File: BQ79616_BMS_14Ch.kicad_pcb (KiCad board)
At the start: 2 copper layers, 100 x 60 mm, 155 parts, among them J1 Conn_02x10_Odd_Even, J2 Conn_02x10_Odd_Even, J3 Conn_Therm, J4 BMS_A_IN, J5 BMS_A_OUT, Q1 MMBT5551

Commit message: Finish positioning of all components Ver1ST
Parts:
- added TP1: TestPoint, TestPoint:TestPoint_THTPad_D1.0mm_Drill0.5mm, F.Cu at (147.1, 103.1)
- C19: renamed from C29; moved to B.Cu
- C20: renamed from C28; moved to B.Cu
- C21: renamed from C27; moved to B.Cu
- C22: renamed from C26; moved to B.Cu
- C23: renamed from C25; moved to B.Cu
- C24: moved to B.Cu
- C25: renamed from C23; moved to B.Cu
- C26: renamed from C22; moved to B.Cu
- C27: renamed from C21; moved to B.Cu
- C28: renamed from C20; moved to B.Cu
- C29: renamed from C19; moved to B.Cu
- C30: renamed from C18; moved to B.Cu
- C31: renamed from C17; moved to B.Cu
- C32: renamed from C16; moved to B.Cu
- JP2: renamed from JP1; moved to B.Cu
- R19: renamed from R2; moved to B.Cu
- R20: renamed from R4; moved to B.Cu
- R21: renamed from R6; moved to B.Cu
- R22: renamed from R8; moved to B.Cu
- R23: renamed from R10; moved to B.Cu
- R24: renamed from R12; moved to B.Cu
- R25: renamed from R14; moved to B.Cu
- R26: renamed from R16; moved to B.Cu
- R27: renamed from R18; moved to B.Cu
- R28: renamed from R20; moved to B.Cu
- R29: renamed from R22; moved to B.Cu
- R30: renamed from R24; moved to B.Cu
- R31: renamed from R26; moved to B.Cu
- R32: renamed from R28; moved to B.Cu
- R33: renamed from R55; moved to B.Cu
- R34: renamed from R32; moved to B.Cu
- R35: renamed from R33; moved to B.Cu
- R36: renamed from R34; moved to B.Cu
- R37: renamed from R35; moved to B.Cu
- R38: renamed from R36; moved to B.Cu
- R39: renamed from R37; moved to B.Cu
- R40: renamed from R38; moved to B.Cu
- R41: renamed from R39; moved to B.Cu
- R43: renamed from R41; moved to B.Cu
- R44: renamed from R42; moved to B.Cu
- R45: renamed from R43; moved to B.Cu
- R46: renamed from R44; moved to B.Cu
- R47: renamed from R45; moved to B.Cu
- R48: renamed from R46; moved to B.Cu
- R49: renamed from R47; moved to B.Cu
- moved H1 102.7 mm to (196.8, 63.2)
- moved F9 93.8 mm to (183.0, 71.8), turned to -90 degrees
- moved H2 88.4 mm to (103.2, 63.2)
- moved R27 82.9 mm to (183.0, 76.8), turned to -90 degrees
- moved DZ1 65.1 mm to (117.0, 116.1)
- moved C12 64.3 mm to (180.0, 68.5), turned to 180 degrees
- moved C26 61.6 mm to (186.0, 81.0), turned to 180 degrees
- moved JP2 60.4 mm to (188.6, 85.3), turned to 90 degrees
- moved DZ2 60.3 mm to (123.0, 116.1)
- moved C13 57.9 mm to (174.0, 68.5), turned to 180 degrees
- moved DZ3 56.0 mm to (129.0, 116.1)
- moved C27 55.1 mm to (180.0, 81.0), turned to 180 degrees
- moved TP3 53.9 mm to (103.7, 86.4)
- moved DZ4 52.3 mm to (135.0, 116.1)
- moved C14 51.4 mm to (168.0, 68.5), turned to 180 degrees
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- renumbered C33 to C1, C9 to C10, C8 to C11, C7 to C12, C6 to C13, C5 to C14, C4 to C15, C3 to C16, C2 to C17, C1 to C18, C34 to C2, C32 to C3, C35 to C33, C36 to C34, C41 to C35, C42 to C36, C43 to C37, C44 to C38, C45 to C39, C15 to C4, C46 to C40, C47 to C41, C48 to C42, C40 to C43, C37 to C44, C38 to C45, C39 to C46, C31 to C47, C61 to C48, C59 to C49, C14 to C5, C60 to C50, C62 to C51, C30 to C52, C13 to C6, C12 to C7, C11 to C8, C10 to C9, DZ14 to DZ1, DZ5 to DZ10, DZ4 to DZ11, DZ3 to DZ12, DZ2 to DZ13, DZ1 to DZ14, DZ13 to DZ2, DZ12 to DZ3, DZ11 to DZ4, DZ10 to DZ5, DZ9 to DZ6, DZ8 to DZ7, DZ7 to DZ8, DZ6 to DZ9, J3 to J1, J1 to J2, J2 to J3, J5 to J4, J4 to J5, JP2 to JP1, R31 to R1, R13 to R10, R15 to R11, R17 to R12, R19 to R13, R21 to R14, R23 to R15, R25 to R16, R27 to R17, R54 to R18, R29 to R2, R30 to R3, R1 to R4, R40 to R42, R3 to R5, R59 to R50, R58 to R51, R60 to R52, R61 to R53, R56 to R54, R57 to R55, R5 to R6, R9 to R8, R11 to R9, TP1 to TP2, TP2 to TP3, TP3 to TP4, TR2 to TR1, TR1 to TR2
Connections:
- C45 pad 1: /ADVV_A -> /AVDD_A
- J2 pad 17: /CELL_A6 -> unconnected-(J2-Pin_17-Pad17)
- J3 pad 1: /CELL_A5 -> /CELL_A6
- J3 pad 12: GND1 -> /CELL_A1
- J3 pad 13: /RX_A -> GND1
- J3 pad 16: /TX_A -> /RX_A
- J3 pad 17: /CVDD_A -> /TX_A
- J3 pad 20: unconnected-(J2-Pin_20-Pad20) (its old number) -> /CVDD_A
- J3 pad 4: /CELL_A4 -> /CELL_A5
- J3 pad 5: /CELL_A3 -> /CELL_A4
- J3 pad 8: /CELL_A2 -> /CELL_A3
- J3 pad 9: /CELL_A1 -> /CELL_A2
- U1 pad 38: /ADVV_A -> /AVDD_A
- U1 pad 49: /ADVV_A -> /DVDD_A
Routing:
- added copper zone on B.Cu, net GND1
- added copper zone on F.Cu, net GND1
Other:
- outline, holes or cut-outs redrawn

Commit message: Save for further try on re-configure of pin position
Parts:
- moved J1 78.8 mm to (192.2, 93.8), turned to -90 degrees
- moved TP4 17.3 mm to (160.6, 85.0)
- moved D1 12.8 mm to (125.1, 104.6)
- moved JP1 12.8 mm to (125.1, 102.5)
- moved C1 12.8 mm to (119.2, 102.5)
- moved R1 12.8 mm to (116.2, 104.0)
- moved R2 12.8 mm to (113.2, 104.0)
- moved R3 12.8 mm to (119.2, 104.0)
- moved TP2 12.8 mm to (122.8, 95.9)
- moved R42 11.3 mm to (157.0, 82.7)
- moved C46 10.6 mm to (134.8, 95.0)
- moved C2 10.6 mm to (136.9, 97.2)
- moved C33 10.6 mm to (135.8, 96.2)
- moved C45 10.6 mm to (132.5, 92.0)
- moved C44 10.6 mm to (131.4, 90.9)
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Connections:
- net /COMHN_A renamed /COMHN
- net /COMHP_A renamed /COMHP
- net /COMLN_A renamed /COMLN
- net /COMLP_A renamed /COMLP
- TR2 pad 1: Net-(R54-Pad2) -> Net-(R55-Pad2)
- TR2 pad 3: Net-(R55-Pad2) -> Net-(R54-Pad2)
- TR2 pad 4: Net-(J5-Pin_2) -> Net-(J5-Pin_1)
- TR2 pad 6: Net-(J5-Pin_1) -> Net-(J5-Pin_2)
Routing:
- net /VC_A6: track 0.00 -> 94.2 mm, vias 0 -> 2
- net /CELL_A7: track 0.00 -> 71.2 mm, vias 0 -> 1
- net /CELL_A8: track 0.00 -> 66.1 mm, vias 0 -> 1
- net /CELL_A9: track 0.00 -> 64.0 mm, vias 0 -> 1
- net /COMHN: track 0.00 -> 60.2 mm, vias 0 -> 2
- net /COMHP: track 0.00 -> 59.1 mm, vias 0 -> 2
- net /CELL_A11: track 0.00 -> 56.2 mm, vias 0 -> 1
- net /CELL_A10: track 0.00 -> 55.7 mm, vias 0 -> 1
- net /CELL_A12: track 0.00 -> 46.1 mm, vias 0 -> 1
- net /CELL_A13: track 0.00 -> 45.3 mm, vias 0 -> 1
- net /CELL_A14: track 0.00 -> 43.2 mm, vias 0 -> 1
- net /COMLN: track 0.00 -> 41.2 mm, vias 0 -> 2
- net /COMLP: track 0.00 -> 40.8 mm, vias 0 -> 2
- net /TSREF_A: track 0.00 -> 35.3 mm, vias 0 -> 1
- net GND1: track 0.00 -> 20.4 mm, vias 0 -> 4
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
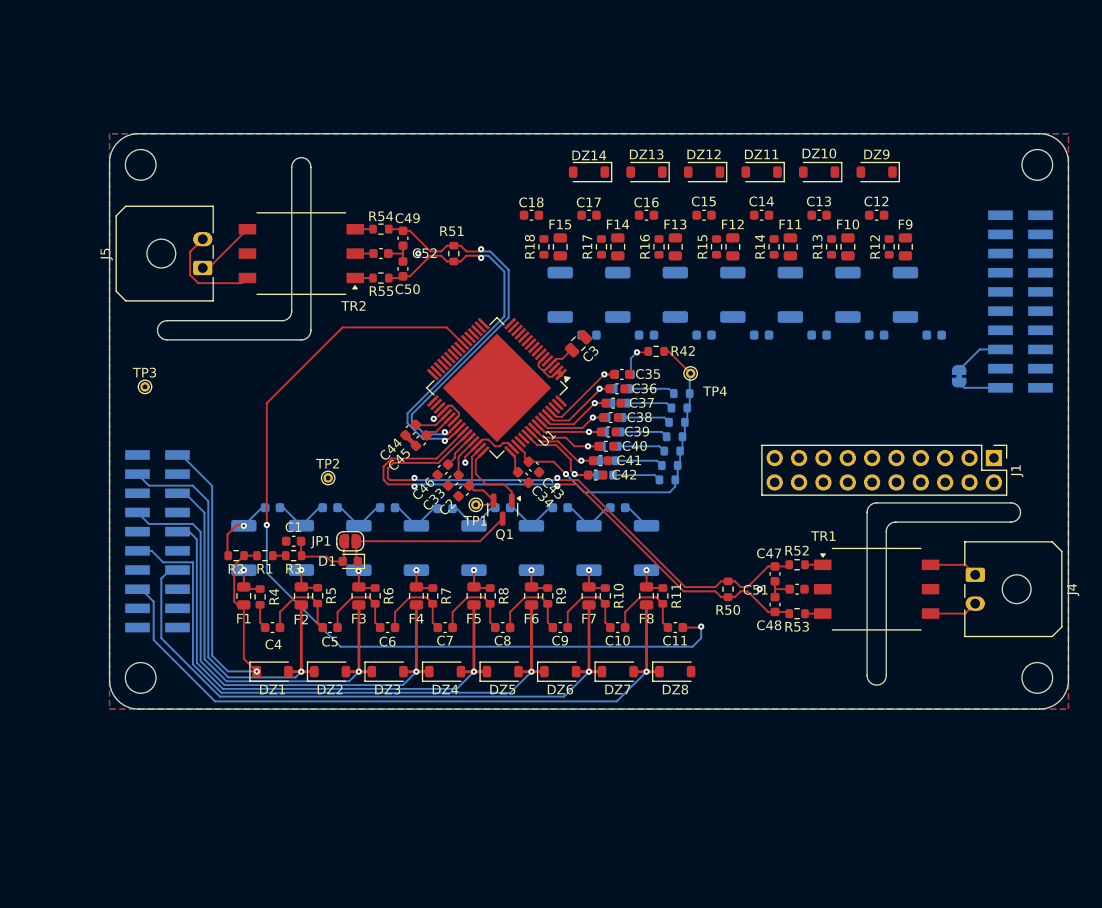
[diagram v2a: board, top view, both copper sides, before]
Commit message: Finish layout for basic need, waited to add logos and labels
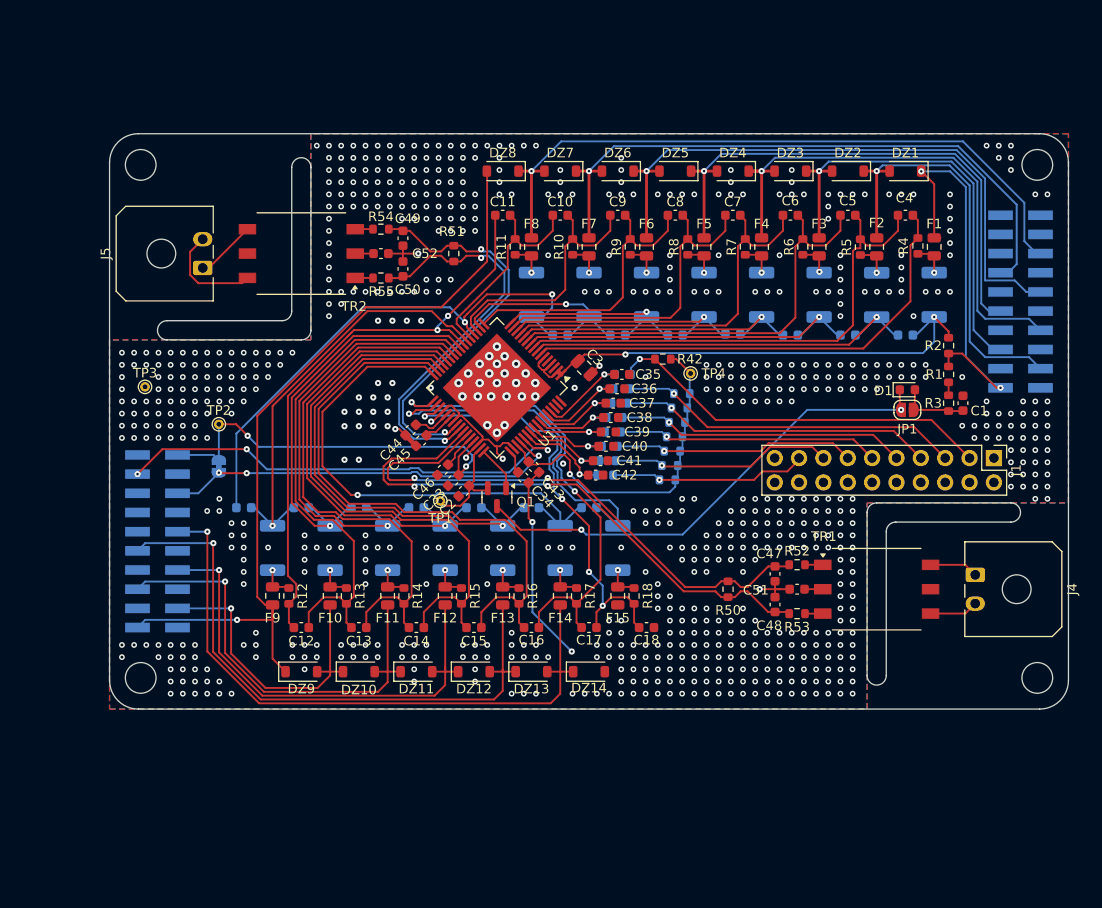
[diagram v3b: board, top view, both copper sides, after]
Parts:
- moved J2 93.4 mm to (195.0, 77.5), turned to 0 degrees
- moved J3 93.4 mm to (105.0, 102.5), turned to 0 degrees
- moved DZ1 84.1 mm to (183.0, 63.9), turned to 180 degrees
- moved F1 80.7 mm to (186.0, 71.8), turned to -90 degrees
- moved DZ9 79.5 mm to (120.0, 116.1), turned to 0 degrees
- moved C4 78.8 mm to (183.0, 68.5), turned to 180 degrees
- moved JP2 77.8 mm to (111.4, 94.7), turned to -90 degrees
- moved R4 77.8 mm to (184.3, 71.7), turned to 90 degrees
- moved R2 77.5 mm to (187.5, 82.1), turned to 90 degrees
- moved R19 76.7 mm to (186.0, 76.8), turned to -90 degrees
- moved F9 75.4 mm to (117.0, 108.2), turned to 90 degrees
- moved DZ2 75.1 mm to (177.0, 63.9), turned to 180 degrees
- moved C26 74.2 mm to (114.0, 99.0), turned to 0 degrees
- moved C12 73.8 mm to (120.0, 111.5), turned to 0 degrees
- moved R1 73.8 mm to (187.5, 85.1), turned to -90 degrees
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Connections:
- U1 pad 16: /C_AB9 -> /CB_A9
- U1 pad 20: unconnected-(U1-CB7-Pad20) -> /CB_A7
- U1 pad 65: (no net) -> GND1
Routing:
- net /CELL_A6: track 0.00 -> 84.4 mm, vias 0 -> 1
- net /CELL_A1: track 0.00 -> 67.0 mm, vias 0 -> 1
- net /CELL_A2: track 0.00 -> 64.1 mm, vias 0 -> 1
- net /VC_A2: track 0.00 -> 62.0 mm
- net /VC_A3: track 0.00 -> 59.0 mm
- net /VC_A4: track 0.00 -> 57.2 mm
- net /VC_A5: track 0.00 -> 54.3 mm
- net /CB_A7: track 3.01 -> 57.0 mm, vias 0 -> 2
- net /CB_A1: track 0.00 -> 53.8 mm, vias 0 -> 1
- net /CELL_A3: track 0.00 -> 50.4 mm, vias 0 -> 1
- net /CB_A2: track 0.00 -> 50.3 mm, vias 0 -> 1
- net /VC_A1: track 0.00 -> 50.0 mm, vias 0 -> 2
- net /TX_A: track 0.00 -> 49.1 mm, vias 0 -> 3
- net /VC_A14: track 2.59 -> 50.4 mm
- net /CB_A3: track 0.00 -> 47.4 mm, vias 0 -> 1
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
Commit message: Fix crystal pinout connection
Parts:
- added G***: LOGO, LOGO, F.Cu at (168.2, 78.4)
- added G***: LOGO, LOGO, F.Cu at (113.3, 99.0)
- added kibuzzard-67A37E08: G***, kibuzzard-67A37E08, B.Cu at (195.0, 88.8)
- added kibuzzard-67A37E45: G***, kibuzzard-67A37E45, B.Cu at (105.0, 91.2)
- added kibuzzard-67A3854A: G***, kibuzzard-67A3854A, F.Cu at (164.5, 85.0)
- added kibuzzard-67A38616: G***, kibuzzard-67A38616, F.Cu at (115.0, 90.2)
- added kibuzzard-67A38633: G***, kibuzzard-67A38633, F.Cu at (106.8, 86.4)
- added kibuzzard-67A38657: G***, kibuzzard-67A38657, F.Cu at (169.9, 91.5)
- added kibuzzard-67A3869A: G***, kibuzzard-67A3869A, F.Cu at (129.8, 98.3)
- added kibuzzard-67A386B0: G***, kibuzzard-67A386B0, F.Cu at (108.9, 66.6)
- added kibuzzard-67A386E1: G***, kibuzzard-67A386E1, F.Cu at (191.1, 113.4)
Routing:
- net /CVDD_A: track 42.8 -> 42.2 mm
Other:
- board text added: "Rev 1.0 Jackempty"

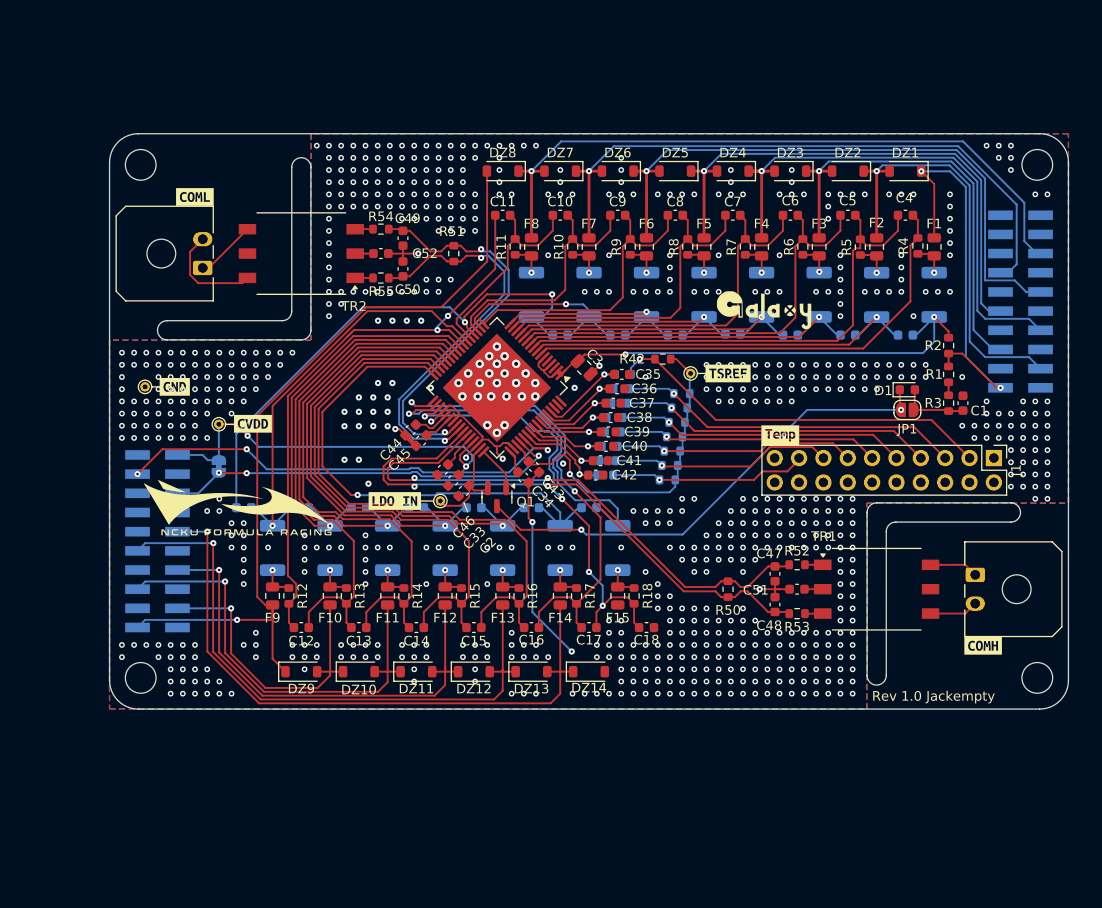
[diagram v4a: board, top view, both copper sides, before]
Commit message: BMS v0.0.2
Use external FET for balancing
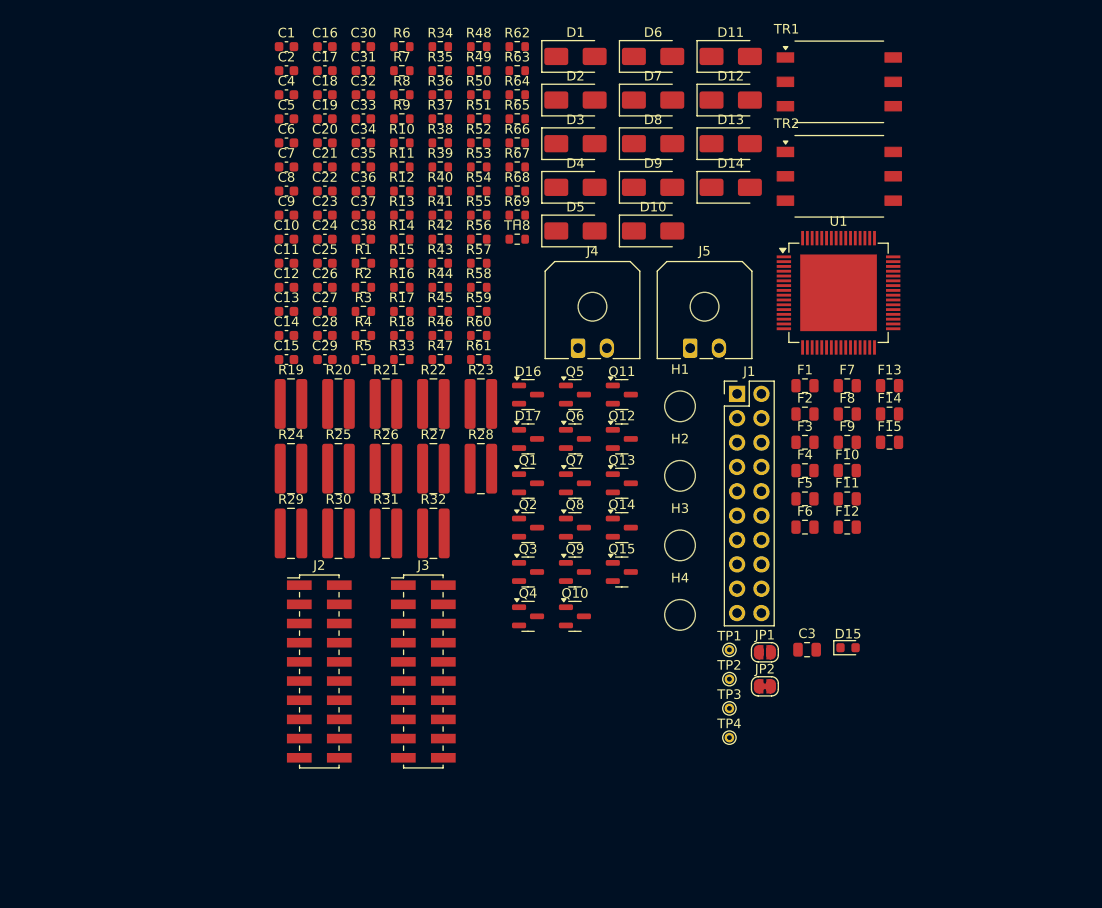
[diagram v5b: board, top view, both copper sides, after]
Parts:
- removed C39, C40, C41, C42, C46: 100n, Capacitor_SMD:C_0603_1608Metric
- removed C43, C44, C45: 1u, Capacitor_SMD:C_0603_1608Metric
- removed C47, C48, C49, C50: 220p, Capacitor_SMD:C_0603_1608Metric
- removed C51, C52: 100p, Capacitor_SMD:C_0603_1608Metric
- removed DZ1, DZ10, DZ11, DZ12, DZ13, DZ14, DZ2, DZ3, DZ4, DZ5, DZ6, DZ7, DZ8, DZ9: MMSZ5232, Diode_SMD:D_SOD-123
- removed G*** (x2): LOGO, LOGO
- removed kibuzzard-67A37E08: G***, kibuzzard-67A37E08
- removed kibuzzard-67A37E45: G***, kibuzzard-67A37E45
- removed kibuzzard-67A3854A: G***, kibuzzard-67A3854A
- removed kibuzzard-67A38616: G***, kibuzzard-67A38616
- removed kibuzzard-67A38633: G***, kibuzzard-67A38633
- removed kibuzzard-67A38657: G***, kibuzzard-67A38657
- removed kibuzzard-67A3869A: G***, kibuzzard-67A3869A
- removed kibuzzard-67A386B0: G***, kibuzzard-67A386B0
- removed kibuzzard-67A386E1: G***, kibuzzard-67A386E1
- added D10: SMA6J5.0CAQ, Diode_SMD:D_SMA, F.Cu at (156.7, 70.1)
- added D11: SMA6J5.0CAQ, Diode_SMD:D_SMA, F.Cu at (164.8, 51.9)
- added D12: SMA6J5.0CAQ, Diode_SMD:D_SMA, F.Cu at (164.8, 56.5)
- added D13: SMA6J5.0CAQ, Diode_SMD:D_SMA, F.Cu at (164.8, 61.0)
- added D14: SMA6J5.0CAQ, Diode_SMD:D_SMA, F.Cu at (164.8, 65.6)
- added D15: LED_PWR, LED_SMD:LED_0603_1608Metric, F.Cu at (177.0, 113.6)
- added D16: DESD12VL2BTQ, Package_TO_SOT_SMD:SOT-23, F.Cu at (143.6, 87.2)
- added D17: DESD12VL2BTQ, Package_TO_SOT_SMD:SOT-23, F.Cu at (143.6, 91.8)
- added D2: SMA6J5.0CAQ, Diode_SMD:D_SMA, F.Cu at (148.6, 56.5)
- added D3: SMA6J5.0CAQ, Diode_SMD:D_SMA, F.Cu at (148.6, 61.0)
- added D4: SMA6J5.0CAQ, Diode_SMD:D_SMA, F.Cu at (148.6, 65.6)
- added D5: SMA6J5.0CAQ, Diode_SMD:D_SMA, F.Cu at (148.6, 70.1)
- added D6: SMA6J5.0CAQ, Diode_SMD:D_SMA, F.Cu at (156.7, 51.9)
- added D7: SMA6J5.0CAQ, Diode_SMD:D_SMA, F.Cu at (156.7, 56.5)
- added D8: SMA6J5.0CAQ, Diode_SMD:D_SMA, F.Cu at (156.7, 61.0)
- added D9: SMA6J5.0CAQ, Diode_SMD:D_SMA, F.Cu at (156.7, 65.6)
- added Q10: DMN2024UQ, Package_TO_SOT_SMD:SOT-23, F.Cu at (148.5, 110.3)
- added Q11: DMN2024UQ, Package_TO_SOT_SMD:SOT-23, F.Cu at (153.4, 87.2)
- added Q12: DMN2024UQ, Package_TO_SOT_SMD:SOT-23, F.Cu at (153.4, 91.8)
- added Q13: DMN2024UQ, Package_TO_SOT_SMD:SOT-23, F.Cu at (153.4, 96.5)
- added Q14: DMN2024UQ, Package_TO_SOT_SMD:SOT-23, F.Cu at (153.4, 101.1)
- added Q15: DMN2024UQ, Package_TO_SOT_SMD:SOT-23, F.Cu at (153.4, 105.7)
- added Q2: DMN2024UQ, Package_TO_SOT_SMD:SOT-23, F.Cu at (143.6, 101.1)
- added Q3: DMN2024UQ, Package_TO_SOT_SMD:SOT-23, F.Cu at (143.6, 105.7)
- added Q4: DMN2024UQ, Package_TO_SOT_SMD:SOT-23, F.Cu at (143.6, 110.3)
- added Q5: DMN2024UQ, Package_TO_SOT_SMD:SOT-23, F.Cu at (148.5, 87.2)
- added Q6: DMN2024UQ, Package_TO_SOT_SMD:SOT-23, F.Cu at (148.5, 91.8)
- added Q7: DMN2024UQ, Package_TO_SOT_SMD:SOT-23, F.Cu at (148.5, 96.5)
- added Q8: DMN2024UQ, Package_TO_SOT_SMD:SOT-23, F.Cu at (148.5, 101.1)
- added Q9: DMN2024UQ, Package_TO_SOT_SMD:SOT-23, F.Cu at (148.5, 105.7)
- added R56: 10k, Resistor_SMD:R_0603_1608Metric, F.Cu at (138.5, 71.0)
- added R57: 10k, Resistor_SMD:R_0603_1608Metric, F.Cu at (138.5, 73.5)
- added R58: 10k, Resistor_SMD:R_0603_1608Metric, F.Cu at (138.5, 76.0)
- added R59: 10k, Resistor_SMD:R_0603_1608Metric, F.Cu at (138.5, 78.5)
- added R60: 10k, Resistor_SMD:R_0603_1608Metric, F.Cu at (138.5, 81.0)
- added R61: 10k, Resistor_SMD:R_0603_1608Metric, F.Cu at (138.5, 83.5)
- added R62: 10k, Resistor_SMD:R_0603_1608Metric, F.Cu at (142.5, 50.9)
- added R63: 10k, Resistor_SMD:R_0603_1608Metric, F.Cu at (142.5, 53.4)
- added R64: 1k, Resistor_SMD:R_0603_1608Metric, F.Cu at (142.5, 55.9)
- added R65: 1k, Resistor_SMD:R_0603_1608Metric, F.Cu at (142.5, 58.5)
- added R66: 49R, Resistor_SMD:R_0603_1608Metric, F.Cu at (142.5, 61.0)
- added R67: 49R, Resistor_SMD:R_0603_1608Metric, F.Cu at (142.5, 63.5)
- added R68: 49R, Resistor_SMD:R_0603_1608Metric, F.Cu at (142.5, 66.0)
- added R69: 49R, Resistor_SMD:R_0603_1608Metric, F.Cu at (142.5, 68.5)
- added TH8: onboard_10k_NTC, Resistor_SMD:R_0603_1608Metric, F.Cu at (142.5, 71.0)
- C19: value 470n -> 4.7u; moved to F.Cu
- C20: value 470n -> 2.2u; moved to F.Cu
- C21, C22, C23, C24, C25, C26, C27, C28, C32: value 470n -> 100n; moved to F.Cu
- C29, C30, C31: value 470n -> 1u; moved to F.Cu
- C33: value 4.7u -> 220p
- C34: value 2.2u -> 220p
- C35, C36: value 100n -> 220p
- C37, C38: value 100n -> 100p
- D1: value LED_PWR -> SMA6J5.0CAQ; footprint LED_SMD:LED_0603_1608Metric -> Diode_SMD:D_SMA
- J2, J3, JP2, R34, R35, R36, R37, R38, R39, R40, R41: moved to F.Cu
- R19, R20, R21, R22, R23, R24, R25, R26, R27, R28, R29, R30, R31, R32: value 10R/0.5W -> 20R/1W; footprint Resistor_SMD:R_2010_5025Metric -> Resistor_SMD:R_1020_2550Metric; moved to F.Cu
- R33: value 10R/0.5W -> 1k; footprint Resistor_SMD:R_2010_5025Metric -> Resistor_SMD:R_0603_1608Metric; moved to F.Cu
- R42: value 10k -> 1k
- R43, R44, R45, R46, R47, R48, R49: value 10k -> 1k; moved to F.Cu
- R52, R53, R54, R55: value 49R -> 1k
- moved J2 82.7 mm to (121.9, 116.1)
- moved C1 79.7 mm to (118.5, 50.9), turned to 0 degrees
- moved TP3 69.6 mm to (164.6, 119.9)
- moved R19 68.0 mm to (118.9, 88.2), turned to 0 degrees
- moved C4 65.8 mm to (118.5, 55.9), turned to 0 degrees
- moved H2 64.9 mm to (159.5, 95.7)
- moved C18 64.9 mm to (122.5, 55.9)
- moved C19 64.6 mm to (122.5, 58.5), turned to 0 degrees
- moved C16 64.3 mm to (122.5, 50.9)
- moved C17 64.3 mm to (122.5, 53.4)
- moved R1 62.1 mm to (126.5, 73.5), turned to 0 degrees
- moved F9 62.0 mm to (176.9, 92.2), turned to 0 degrees
- moved R3 61.8 mm to (126.5, 78.5), turned to 0 degrees
- moved JP2 61.4 mm to (168.3, 117.6), turned to 0 degrees
- moved R2 61.3 mm to (126.5, 76.0), turned to 0 degrees
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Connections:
- C1 pad 2: Net-(D1-A) -> Net-(D15-A)
- C19 pad 1: /BAT_A -> /CVDD_A
- C19 pad 2: /CB_A13 -> GND1
- C20 pad 1: /CB_A13 -> /DVDD_A
- C20 pad 2: /CB_A12 -> GND1
- C21 pad 1: /CB_A12 -> /GPIO_A1
- C21 pad 2: /CB_A11 -> GND1
- C22 pad 1: /CB_A11 -> /GPIO_A2
- C22 pad 2: /CB_A10 -> GND1
- C23 pad 1: /CB_A10 -> /GPIO_A3
- C23 pad 2: /CB_A9 -> GND1
- C24 pad 1: /CB_A9 -> /GPIO_A4
- C24 pad 2: /CB_A8 -> GND1
- C25 pad 1: /CB_A8 -> /GPIO_A5
- C25 pad 2: /CB_A7 -> GND1
- C26 pad 1: /CB_A7 -> /GPIO_A6
- C26 pad 2: /CB_A6 -> GND1
- C27 pad 1: /CB_A6 -> /GPIO_A7
- C27 pad 2: /CB_A5 -> GND1
- C28 pad 1: /CB_A5 -> /GPIO_A8
- C28 pad 2: /CB_A4 -> GND1
- C29 pad 1: /CB_A4 -> /TSREF_A
- C29 pad 2: /CB_A3 -> GND1
- C30 pad 1: /CB_A3 -> /REFHP_A
- C30 pad 2: /CB_A2 -> GND1
- C31 pad 1: /CB_A2 -> /AVDD_A
- C31 pad 2: /CB_A1 -> GND1
- C32 pad 1: /CB_A1 -> /NEG5V_A
- C32 pad 2: /CB_A0 -> GND1
- C33 pad 1: /CVDD_A -> /COMHP
- C34 pad 1: /DVDD_A -> /COMHN
- C35 pad 1: /GPIO_A1 -> /COMLP
- C36 pad 1: /GPIO_A2 -> /COMLN
- C37 pad 1: /GPIO_A3 -> Net-(C37-Pad1)
- C38 pad 1: /GPIO_A4 -> Net-(C38-Pad1)
- D1 pad 1: Net-(D1-K) -> Net-(D1-A1)
- D1 pad 2: Net-(D1-A) -> Net-(D1-A2)
- F1 pad 2: Net-(F1-Pad2) -> Net-(D1-A2)
- F10 pad 2: Net-(F10-Pad2) -> Net-(D10-A2)
- F11 pad 2: Net-(F11-Pad2) -> Net-(D10-A1)
- F12 pad 2: Net-(F12-Pad2) -> Net-(D11-A1)
- F13 pad 2: Net-(F13-Pad2) -> Net-(D12-A1)
- F14 pad 2: Net-(F14-Pad2) -> Net-(D13-A1)
- F15 pad 2: Net-(F15-Pad2) -> Net-(D14-A1)
- F2 pad 2: Net-(F2-Pad2) -> Net-(D1-A1)
- F3 pad 2: Net-(F3-Pad2) -> Net-(D2-A1)
- F4 pad 2: Net-(F4-Pad2) -> Net-(D3-A1)
- F5 pad 2: Net-(F5-Pad2) -> Net-(D4-A1)
- F6 pad 2: Net-(F6-Pad2) -> Net-(D5-A1)
- F7 pad 2: Net-(F7-Pad2) -> Net-(D6-A1)
- F8 pad 2: Net-(F8-Pad2) -> Net-(D7-A1)
- F9 pad 2: Net-(F9-Pad2) -> Net-(D8-A1)
- J1 pad 17: /TH_A8 -> unconnected-(J1-Pin_17-Pad17)
- JP1 pad 1: Net-(D1-A) -> Net-(D15-A)
- JP1 pad 2: Net-(D1-K) -> Net-(D15-K)
- Q1 pad 3: Net-(D1-K) -> Net-(D15-K)
- R1 pad 1: /CELL_A14 -> Net-(D1-A2)
- R10 pad 1: Net-(F7-Pad2) -> Net-(D6-A1)
- R11 pad 1: Net-(F8-Pad2) -> Net-(D7-A1)
- R12 pad 1: Net-(F9-Pad2) -> Net-(D8-A1)
- R13 pad 1: Net-(F10-Pad2) -> Net-(D10-A2)
- R14 pad 1: Net-(F11-Pad2) -> Net-(D10-A1)
- R15 pad 1: Net-(F12-Pad2) -> Net-(D11-A1)
- R16 pad 1: Net-(F13-Pad2) -> Net-(D12-A1)
- R17 pad 1: Net-(F14-Pad2) -> Net-(D13-A1)
- R18 pad 1: Net-(F15-Pad2) -> Net-(D14-A1)
- R19 pad 1: Net-(F1-Pad2) -> Net-(D1-A2)
- R19 pad 2: /BAT_A -> Net-(Q2-D)
- R2 pad 1: /CELL_A14 -> Net-(D1-A2)
- R20 pad 1: Net-(F2-Pad2) -> Net-(D1-A1)
- R20 pad 2: /CB_A13 -> Net-(Q3-D)
- R21 pad 1: Net-(F3-Pad2) -> Net-(D2-A1)
- R21 pad 2: /CB_A12 -> Net-(Q4-D)
- R22 pad 1: Net-(F4-Pad2) -> Net-(D3-A1)
- R22 pad 2: /CB_A11 -> Net-(Q5-D)
- R23 pad 1: Net-(F5-Pad2) -> Net-(D4-A1)
- R23 pad 2: /CB_A10 -> Net-(Q6-D)
- R24 pad 1: Net-(F6-Pad2) -> Net-(D5-A1)
- R24 pad 2: /CB_A9 -> Net-(Q7-D)
- R25 pad 1: Net-(F7-Pad2) -> Net-(D6-A1)
- R25 pad 2: /CB_A8 -> Net-(Q8-D)
- R26 pad 1: Net-(F8-Pad2) -> Net-(D7-A1)
- R26 pad 2: /CB_A7 -> Net-(Q9-D)
- R27 pad 1: Net-(F9-Pad2) -> Net-(D8-A1)
- R27 pad 2: /CB_A6 -> Net-(Q10-D)
- R28 pad 1: Net-(F10-Pad2) -> Net-(D10-A2)
- R28 pad 2: /CB_A5 -> Net-(Q11-D)
- R29 pad 1: Net-(F11-Pad2) -> Net-(D10-A1)
- R29 pad 2: /CB_A4 -> Net-(Q12-D)
- R3 pad 2: Net-(D1-A) -> Net-(D15-A)
- R30 pad 1: Net-(F12-Pad2) -> Net-(D11-A1)
- R30 pad 2: /CB_A3 -> Net-(Q13-D)
- R31 pad 1: Net-(F13-Pad2) -> Net-(D12-A1)
- R31 pad 2: /CB_A2 -> Net-(Q14-D)
- R32 pad 1: Net-(F14-Pad2) -> Net-(D13-A1)
- R32 pad 2: /CB_A1 -> Net-(Q15-D)
- R33 pad 1: Net-(F15-Pad2) -> Net-(D1-A2)
- R33 pad 2: /CB_A0 -> /BAT_A
- R34 pad 1: /GPIO_A1 -> Net-(D1-A1)
- R34 pad 2: /TH_A1 -> /CB_A13
- R35 pad 1: /GPIO_A2 -> Net-(D2-A1)
- R35 pad 2: /TH_A2 -> /CB_A12
- R36 pad 1: /GPIO_A3 -> Net-(D3-A1)
- R36 pad 2: /TH_A3 -> /CB_A11
- R37 pad 1: /GPIO_A4 -> Net-(D4-A1)
- R37 pad 2: /TH_A4 -> /CB_A10
- R38 pad 1: /GPIO_A5 -> Net-(D5-A1)
- R38 pad 2: /TH_A5 -> /CB_A9
- R39 pad 1: /GPIO_A6 -> Net-(D6-A1)
- R39 pad 2: /TH_A6 -> /CB_A8
- R4 pad 1: Net-(F1-Pad2) -> Net-(D1-A2)
- R40 pad 1: /GPIO_A7 -> Net-(D7-A1)
- R40 pad 2: /TH_A7 -> /CB_A7
- R41 pad 1: /GPIO_A8 -> Net-(D8-A1)
- R41 pad 2: /TH_A8 -> /CB_A6
- R42 pad 1: /TSREF_A -> Net-(D10-A2)
- R42 pad 2: /TH_A1 -> /CB_A5
- R43 pad 1: /TSREF_A -> Net-(D10-A1)
- R43 pad 2: /TH_A2 -> /CB_A4
- R44 pad 1: /TSREF_A -> Net-(D11-A1)
- R44 pad 2: /TH_A3 -> /CB_A3
- R45 pad 1: /TSREF_A -> Net-(D12-A1)
- R45 pad 2: /TH_A4 -> /CB_A2
- R46 pad 1: /TSREF_A -> Net-(D13-A1)
- R46 pad 2: /TH_A5 -> /CB_A1
- R47 pad 1: /TSREF_A -> Net-(D14-A1)
- R47 pad 2: /TH_A6 -> /CB_A0
- R48 pad 1: /TSREF_A -> /GPIO_A1
- R48 pad 2: /TH_A7 -> /TH_A1
- R49 pad 1: /TSREF_A -> /GPIO_A2
- R49 pad 2: /TH_A8 -> /TH_A2
- R5 pad 1: Net-(F2-Pad2) -> Net-(D1-A1)
- R50 pad 1: /COMHP -> /GPIO_A3
- R50 pad 2: /COMHN -> /TH_A3
- R51 pad 1: /COMLP -> /GPIO_A4
- R51 pad 2: /COMLN -> /TH_A4
- R52 pad 1: /COMHP -> /GPIO_A5
- R52 pad 2: Net-(R52-Pad2) -> /TH_A5
- R53 pad 1: /COMHN -> /GPIO_A6
- R53 pad 2: Net-(R53-Pad2) -> /TH_A6
- R54 pad 1: /COMLP -> /GPIO_A7
- R54 pad 2: Net-(R54-Pad2) -> /TH_A7
- R55 pad 1: /COMLN -> /GPIO_A8
- R55 pad 2: Net-(R55-Pad2) -> /TH_A8
- R6 pad 1: Net-(F3-Pad2) -> Net-(D2-A1)
- R7 pad 1: Net-(F4-Pad2) -> Net-(D3-A1)
- R8 pad 1: Net-(F5-Pad2) -> Net-(D4-A1)
- R9 pad 1: Net-(F6-Pad2) -> Net-(D5-A1)
- TR1 pad 1: Net-(R52-Pad2) -> Net-(R66-Pad2)
- TR1 pad 2: Net-(C51-Pad1) -> Net-(C37-Pad1)
- TR1 pad 3: Net-(R53-Pad2) -> Net-(R67-Pad2)
- TR2 pad 1: Net-(R55-Pad2) -> Net-(R68-Pad2)
- TR2 pad 2: Net-(C52-Pad1) -> Net-(C38-Pad1)
- TR2 pad 3: Net-(R54-Pad2) -> Net-(R69-Pad2)
- TR2 pad 4: Net-(J5-Pin_1) -> Net-(J5-Pin_2)
- TR2 pad 6: Net-(J5-Pin_2) -> Net-(J5-Pin_1)
- U1 pad 65: GND1 -> (no net)
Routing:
- net /CELL_A6: track 84.4 -> 0.00 mm, vias 1 -> 0
- net /CELL_A7: track 71.2 -> 0.00 mm, vias 1 -> 0
- net /CELL_A1: track 67.0 -> 0.00 mm, vias 1 -> 0
- net /CELL_A8: track 66.1 -> 0.00 mm, vias 1 -> 0
- net /CELL_A2: track 64.1 -> 0.00 mm, vias 1 -> 0
- net /CELL_A9: track 64.0 -> 0.00 mm, vias 1 -> 0
- net /VC_A2: track 62.0 -> 0.00 mm
- net /VC_A6: track 61.9 -> 0.00 mm, vias 2 -> 0
- net /COMHN: track 60.2 -> 0.00 mm, vias 2 -> 0
- net /COMHP: track 59.1 -> 0.00 mm, vias 2 -> 0
- net /VC_A3: track 59.0 -> 0.00 mm
- net /VC_A4: track 57.2 -> 0.00 mm
- net /CB_A7: track 57.0 -> 0.00 mm, vias 2 -> 0
- net /CELL_A11: track 56.2 -> 0.00 mm, vias 1 -> 0
- net /CELL_A10: track 55.7 -> 0.00 mm, vias 1 -> 0
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- removed copper zone on B.Cu, net GND1
- removed copper zone on F.Cu, net GND1
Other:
- board outline removed
- board text removed: "Rev 1.0 Jackempty"
